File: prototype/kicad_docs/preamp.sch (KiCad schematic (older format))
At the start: 31 parts, among them U1 12AX7, U2 12AX7

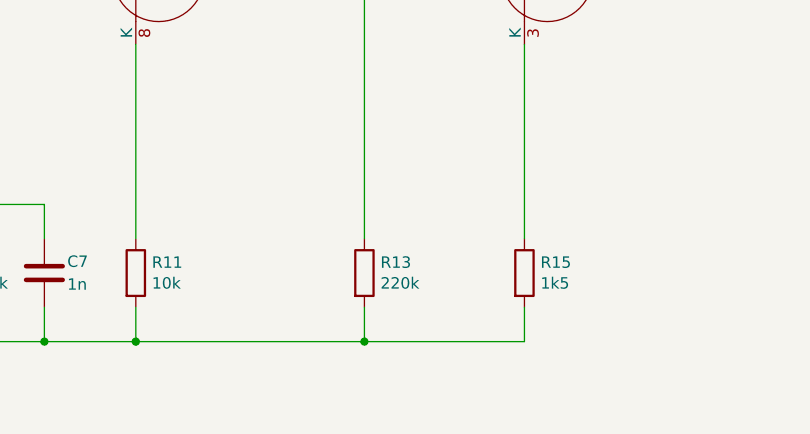
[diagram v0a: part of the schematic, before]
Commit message: reduce gain in last preamp stage
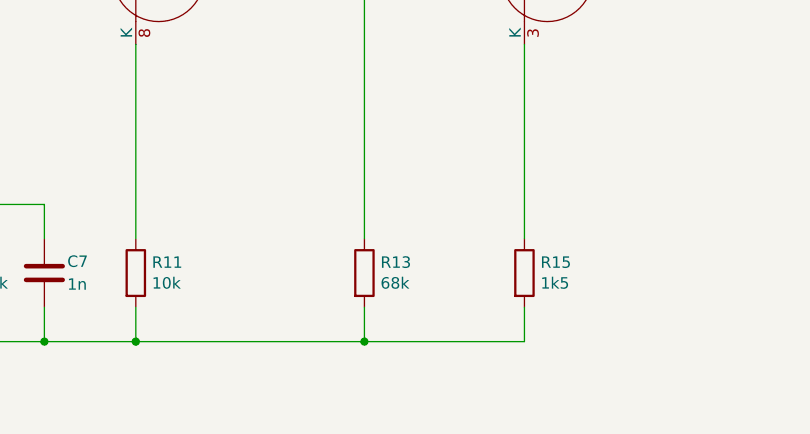
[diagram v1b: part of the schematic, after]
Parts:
- R13: value 220k -> 68k
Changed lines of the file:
@@
 P 8400 5700
 F 0 "R13" H 8470 5746 50  0000 L CNN
-F 1 "220k" H 8470 5655 50  0000 L CNN
+F 1 "68k" H 8470 5655 50  0000 L CNN
 F 2 "" V 8330 5700 50  0001 C CNN
 F 3 "~" H 8400 5700 50  0001 C CNN

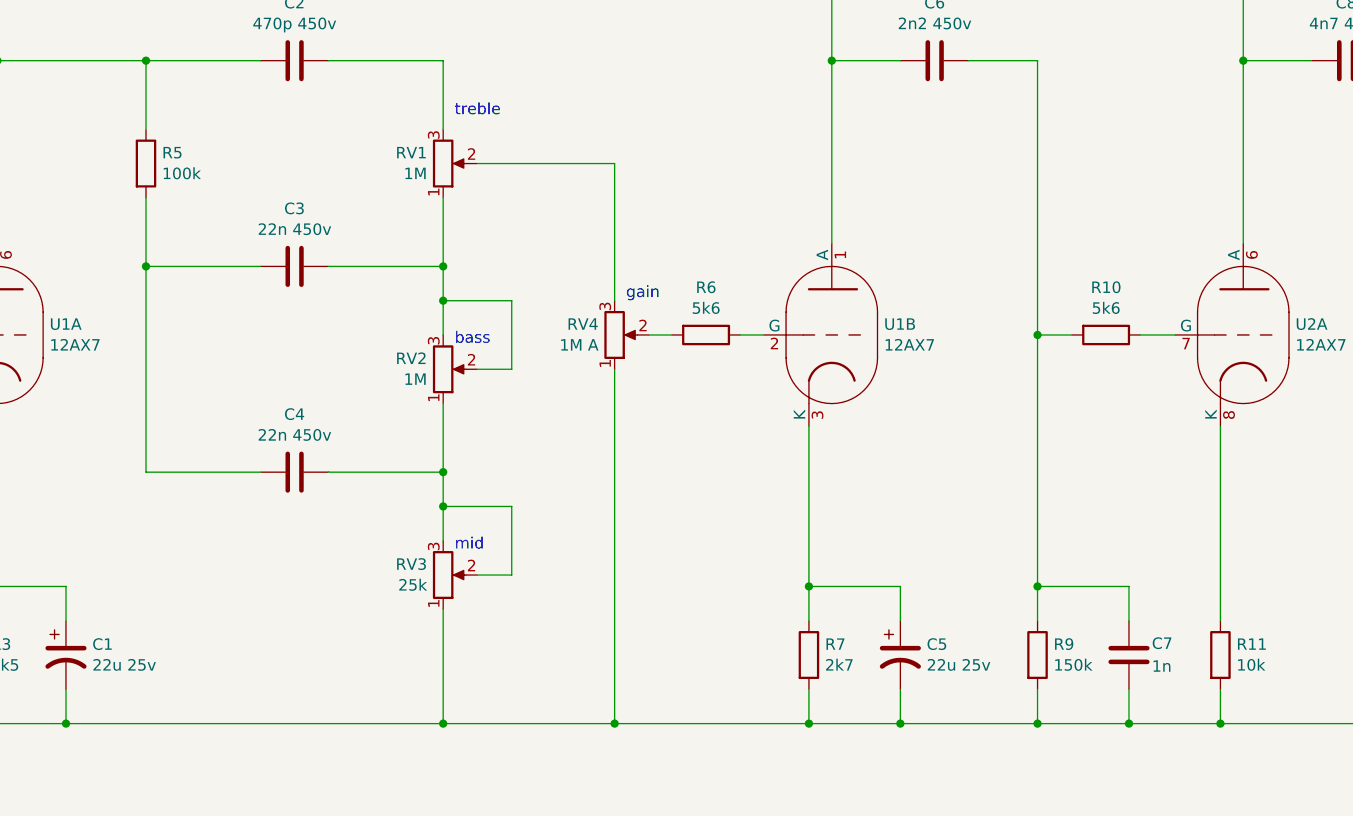
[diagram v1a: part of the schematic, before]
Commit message: tweak prototype, add to proto write-up
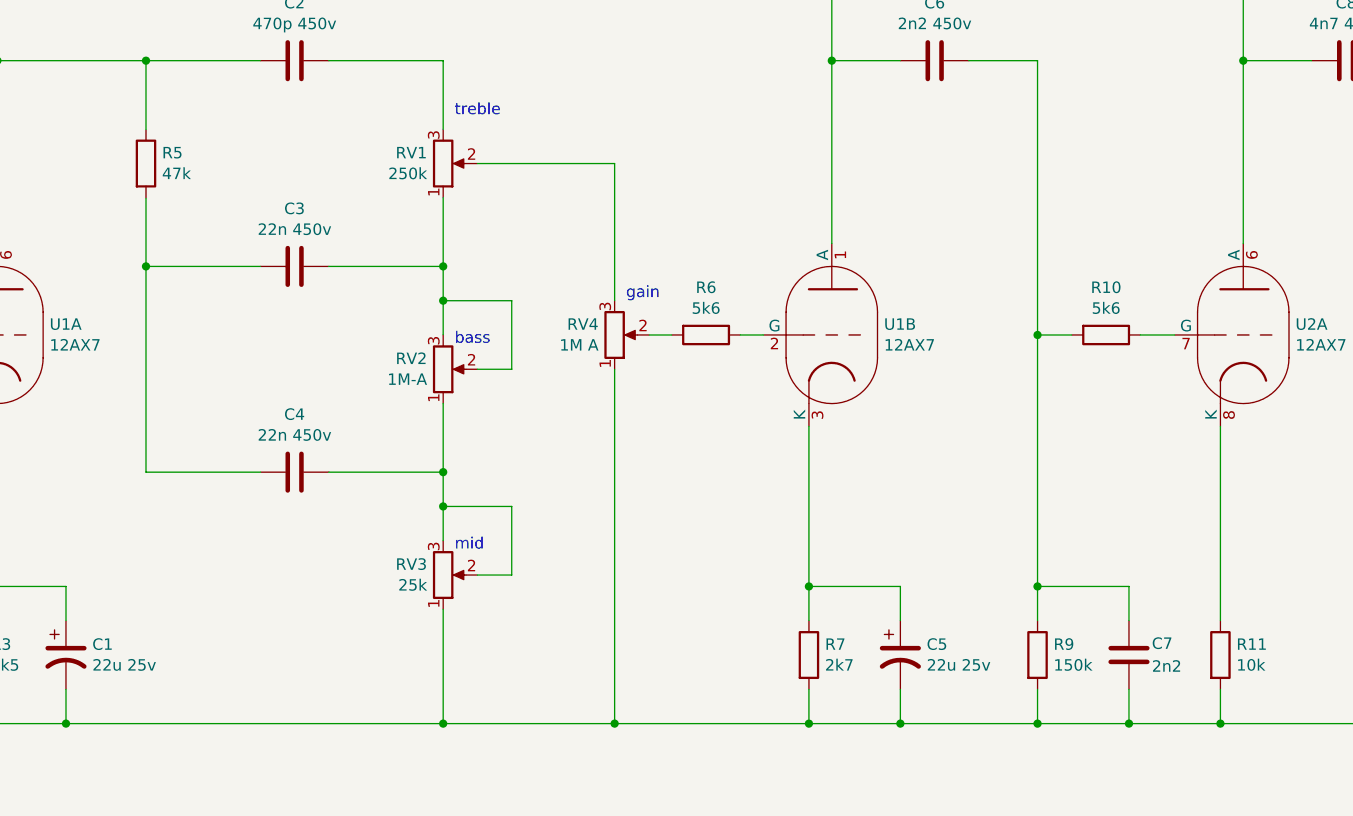
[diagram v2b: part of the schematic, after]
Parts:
- C7: value 1n -> 2n2
- R5: value 100k -> 47k
- RV1: value 1M -> 250k
- RV2: value 1M -> 1M-A
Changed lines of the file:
@@
 P 2700 3550
 F 0 "R5" H 2770 3596 50  0000 L CNN
-F 1 "100k" H 2770 3505 50  0000 L CNN
+F 1 "47k" H 2770 3505 50  0000 L CNN
 F 2 "" V 2630 3550 50  0001 C CNN
 F 3 "~" H 2700 3550 50  0001 C CNN
@@
 P 4000 3550
 F 0 "RV1" H 3930 3504 50  0000 R CNN
-F 1 "1M" H 3930 3595 50  0000 R CNN
+F 1 "250k" H 3930 3595 50  0000 R CNN
 F 2 "" H 4000 3550 50  0001 C CNN
 F 3 "~" H 4000 3550 50  0001 C CNN
@@
 P 4000 4450
 F 0 "RV2" H 3930 4404 50  0000 R CNN
-F 1 "1M" H 3930 4495 50  0000 R CNN
+F 1 "1M-A" H 3930 4495 50  0000 R CNN
 F 2 "" H 4000 4450 50  0001 C CNN
 F 3 "~" H 4000 4450 50  0001 C CNN
@@
 P 7000 5700
 F 0 "C7" H 7100 5750 50  0000 L CNN
-F 1 "1n" H 7100 5650 50  0000 L CNN
+F 1 "2n2" H 7100 5650 50  0000 L CNN
 F 2 "" H 7038 5550 50  0001 C CNN
 F 3 "~" H 7000 5700 50  0001 C CNN
